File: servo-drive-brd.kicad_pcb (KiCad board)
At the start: 2 copper layers, 54.6 x 33 mm, 9 parts, among them CON1 BARREL_JACK, P1 CONN_01X03, U1 LM555N

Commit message: Add gerber files and pcb layout
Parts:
- moved R1 143.4 mm to (156.2, 95.2)
- moved C1 140.2 mm to (171.4, 118.1)
- moved C2 140.2 mm to (177.8, 118.1)
- moved CON1 140.2 mm to (137.1, 94.8)
- moved D1 140.2 mm to (178.0, 101.1)
- moved P1 140.2 mm to (140.9, 106.3)
- moved PTV09A-2 140.2 mm to (171.5, 91.8)
- moved R2 140.2 mm to (175.9, 111.1)
- moved U1 140.2 mm to (154.9, 112.6)
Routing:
- net Net-(PTV09A-2-Pad1): track 14.1 -> 10.3 mm
- net +5V: track 45.6 -> 47.8 mm
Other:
- board size 54.6 x 33 mm -> 54.6 x 34.3 mm
- rule trace_min: 0.2 -> 0.1524
- rule via_min_drill: 0.3 -> 0.3556
- rule via_min_size: 0.4 -> 0.1778

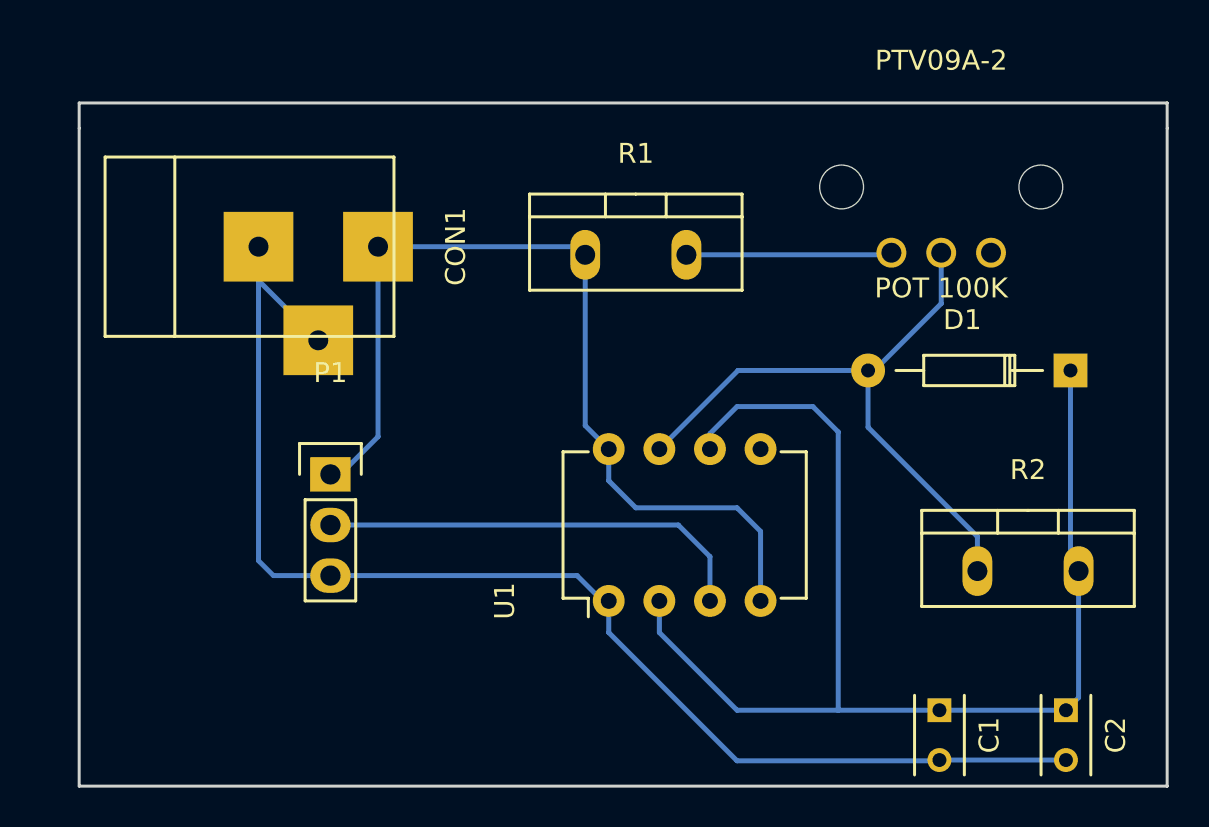
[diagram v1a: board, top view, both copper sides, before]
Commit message: Final version (hopefully, fingers crossed) with a linear power regulator, and a horizontally mounted pot (facing the right way)
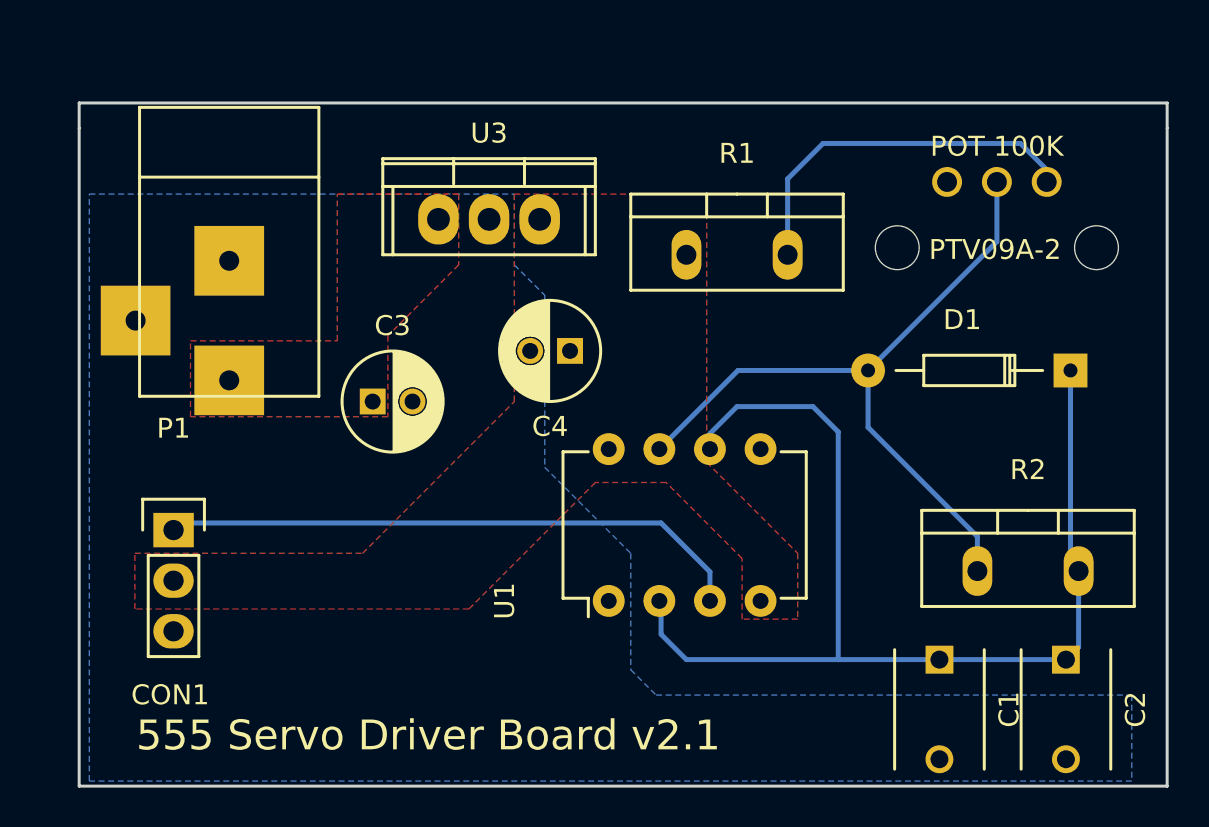
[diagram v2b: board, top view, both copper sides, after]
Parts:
- added C3: 10 uF, Capacitors_ThroughHole:C_Radial_D5_L11_P2, F.Cu at (143.0, 102.6)
- added C4: 10 uF, Capacitors_ThroughHole:C_Radial_D5_L11_P2, F.Cu at (152.9, 100.1)
- added U3: LM7805CT, TO-220, F.Cu at (148.8, 93.5)
- C1, C2: footprint Capacitors_ThroughHole:C_Rect_L4_W2.5_P2.5 -> Capacitors_ThroughHole:C_Disc_D6_P5
- moved P1 8.36 mm to (133.0, 109.1)
- moved R1 5.08 mm to (161.3, 95.2)
- moved PTV09A-2 4.13 mm to (174.3, 94.9), turned to 180 degrees
- moved C1 2.54 mm to (171.4, 115.6)
- moved C2 2.54 mm to (177.8, 115.6)
- moved CON1 1.37 mm to (135.8, 95.4), turned to 270 degrees
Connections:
- CON1 pad 1: +5V -> Net-(C3-Pad1)
- P1 pad 1: +5V -> Net-(P1-Pad1)
- P1 pad 2: Net-(P1-Pad2) -> +5V
- U1 pad 3: Net-(P1-Pad2) -> Net-(P1-Pad1)
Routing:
- net GND: track 67.3 -> 2.07 mm
- net +5V: track 47.8 -> 1.07 mm
- net Net-(P1-Pad1): track 0.00 -> 30.0 mm
- net Net-(P1-Pad2): track 21.9 -> 0.00 mm
- net Net-(PTV09A-2-Pad1): track 10.3 -> 18.9 mm
- net Net-(C1-Pad1): track 63.9 -> 57.8 mm
- net Net-(D1-Pad2): track 32.1 -> 36.9 mm
- added copper zone on F.Cu, net +5V
- added copper zone on B.Cu, net GND
- added copper zone on F.Cu, net Net-(C3-Pad1)
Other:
- board text added: "555 Servo Driver Board v2.1"
